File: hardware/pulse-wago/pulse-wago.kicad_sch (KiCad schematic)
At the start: 44 parts, among them J101 Cortex, SW101 SKSG, SW102 SKSG, U101 ATSAMD51J, U102 TPS78433QWDRBRQ1, Y101 32k768

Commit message: Refresh
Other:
- note added: "Solenoid Channels / Power +28V"
- note removed: "Solenoid Channels / Power +24V"
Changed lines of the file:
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@@
 		)
 	)
-	(text "Solenoid Channels / Power +24V"
+	(text "Solenoid Channels / Power +28V"
 		(exclude_from_sim no)
 		(at 153.035 16.51 0)

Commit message: Refresh
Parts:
- C107, C108: Manufacturer YAGEO -> TDK; Mouser 603-CC603JRNPO9BN180 -> 810-CGA3E2C0G1H180J; Product CC0603JRNPO9BN180 -> CGA3E2C0G1H180J080AA
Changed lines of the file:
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@@
 	(title_block
 		(title "V2 pulse WAGO")
-		(date "2026-02-10")
+		(date "2026-03-04")
 		(rev "2025-10-27")
 		(company "Versio Duo")
@@
 		(at 184.785 170.18 0)
 		(unit 1)
-		(exclude_from_sim yes)
+		(exclude_from_sim no)
 		(in_bom no)
 		(on_board yes)
@@
 			)
 		)
+		(property "Sim.Enable" "0"
+			(at 184.785 170.18 0)
+			(effects
+				(font
+					(size 1.27 1.27)
+				)
+				(hide yes)
+			)
+		)
 		(instances
 			(project "pulse"
@@
 		(at 218.44 151.13 0)
 		(unit 1)
-		(exclude_from_sim yes)
+		(exclude_from_sim no)
 		(in_bom no)
 		(on_board yes)
@@
 			)
 		)
+		(property "Sim.Enable" "0"
+			(at 218.44 151.13 0)
+			(effects
+				(font
+					(size 1.27 1.27)
+				)
+				(hide yes)
+			)
+		)
 		(instances
 			(project "pulse"
@@
 		(at 184.785 151.765 0)
 		(unit 1)
-		(exclude_from_sim yes)
+		(exclude_from_sim no)
 		(in_bom no)
 		(on_board yes)
@@
 			)
 		)
+		(property "Sim.Enable" "0"
+			(at 184.785 151.765 0)
+			(effects
+				(font
+					(size 1.27 1.27)
+				)
+				(hide yes)
+			)
+		)
 		(instances
 			(project "pulse"
@@
 		(at 218.44 157.48 0)
 		(unit 1)
-		(exclude_from_sim yes)
+		(exclude_from_sim no)
 		(in_bom no)
 		(on_board yes)
@@
 			)
 		)
+		(property "Sim.Enable" "0"
+			(at 218.44 157.48 0)
+			(effects
+				(font
+					(size 1.27 1.27)
+				)
+				(hide yes)
+			)
+		)
 		(instances
 			(project ""
@@
 			)
 		)
-		(property "Mouser" "603-CC603JRNPO9BN180"
+		(property "Mouser" "810-CGA3E2C0G1H180J"
 			(at 26.67 70.358 0)
 			(effects
@@
 			)
 		)
-		(property "Product" "CC0603JRNPO9BN180"
+		(property "Product" "CGA3E2C0G1H180J080AA"
 			(at 26.67 67.564 0)
 			(effects
@@
 			)
 		)
-		(property "Manufacturer" "YAGEO"
+		(property "Manufacturer" "TDK"
 			(at 26.67 64.77 0)
 			(effects
@@
 		(at 158.75 161.925 0)
 		(unit 1)
-		(exclude_from_sim yes)
+		(exclude_from_sim no)
 		(in_bom no)
 		(on_board yes)
@@
 			)
 		)
+		(property "Sim.Enable" "0"
+			(at 158.75 161.925 0)
+			(effects
+				(font
+					(size 1.27 1.27)
+				)
+				(hide yes)
+			)
+		)
 		(instances
 			(project "pulse"
@@
 			)
 		)
-		(property "Mouser" "603-CC603JRNPO9BN180"
+		(property "Mouser" "810-CGA3E2C0G1H180J"
 			(at 21.59 70.358 0)
 			(effects
@@
 			)
 		)
-		(property "Product" "CC0603JRNPO9BN180"
+		(property "Product" "CGA3E2C0G1H180J080AA"
 			(at 21.59 67.564 0)
 			(effects
@@
 			)
 		)
-		(property "Manufacturer" "YAGEO"
+		(property "Manufacturer" "TDK"
 			(at 21.59 64.77 0)
 			(effects
@@
 		(at 218.44 163.83 0)
 		(unit 1)
-		(exclude_from_sim yes)
+		(exclude_from_sim no)
 		(in_bom no)
 		(on_board yes)
@@
 			)
 		)
+		(property "Sim.Enable" "0"
+			(at 218.44 163.83 0)
+			(effects
+				(font
+					(size 1.27 1.27)
+				)
+				(hide yes)
+			)
+		)
 		(instances
 			(project ""
@@
 		(at 184.785 161.29 0)
 		(unit 1)
-		(exclude_from_sim yes)
+		(exclude_from_sim no)
 		(in_bom no)
 		(on_board yes)
@@
 			(at 184.785 161.29 0)
 			(effects
+				(font
+					(size 1.27 1.27)
+				)
+				(hide yes)
+			)
+		)
+		(property "Sim.Enable" "0"
+			(at 184.785 161.29 0)
+			(effects

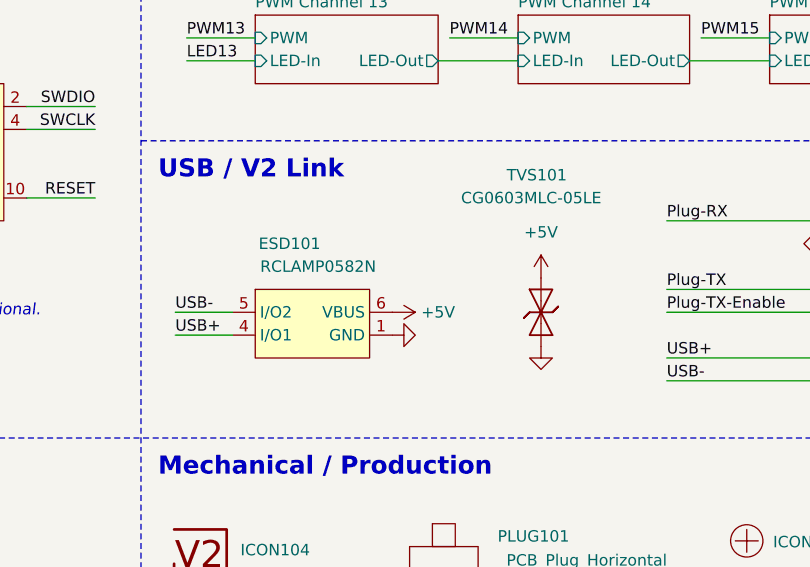
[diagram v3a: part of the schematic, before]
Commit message: Update ESD suppressor
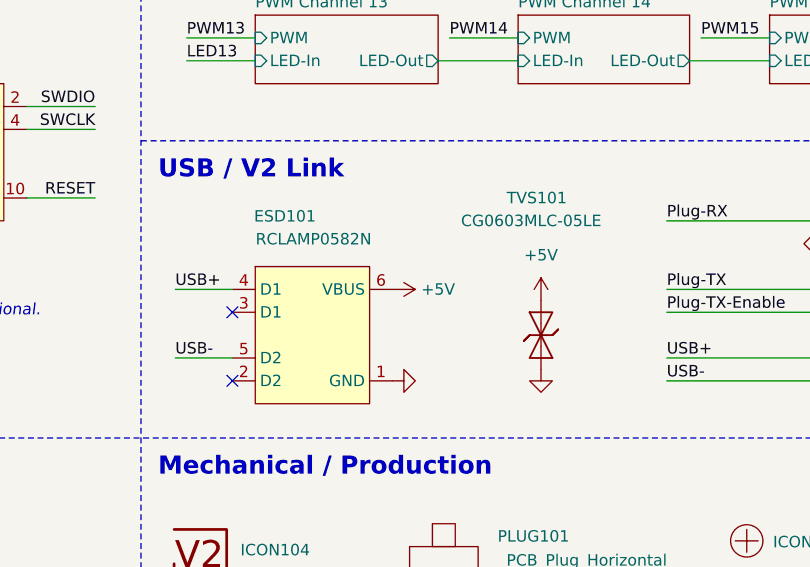
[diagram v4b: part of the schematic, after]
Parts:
- INFO102: value (none) -> ~
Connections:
- no-connect marks 16 -> 18
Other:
- moved on the sheet: TVS101

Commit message: Replace diode
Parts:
- INFO102: value ~ -> (none)

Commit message: Update
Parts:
- C101: renamed from C107; Id (none) -> Capacitor:${SYMBOL_NAME}; Rating (none) -> 50V
- C102: renamed from C108; Id (none) -> Capacitor:${SYMBOL_NAME}; Rating (none) -> 50V
- C103: renamed from C109; Id (none) -> Capacitor:${SYMBOL_NAME}
- C104: renamed from C101; Id (none) -> Capacitor:${SYMBOL_NAME}
- C105: renamed from C110; Id (none) -> Capacitor:${SYMBOL_NAME}
- C106: renamed from C102; Id (none) -> Capacitor:${SYMBOL_NAME}
- C107: renamed from C103; Id (none) -> Capacitor:${SYMBOL_NAME}
- C108: renamed from C104; Id (none) -> Capacitor:${SYMBOL_NAME}
- C109: renamed from C105; Id (none) -> Capacitor:${SYMBOL_NAME}
- C110: renamed from C106; Id (none) -> Capacitor:${SYMBOL_NAME}
- D101: renamed from D102; Id (none) -> LED:${SYMBOL_NAME}; Rating (none) -> 15mA
- D102: renamed from D101; Id (none) -> LED:${SYMBOL_NAME}; Rating (none) -> 605nm
- D103: Id (none) -> LED:${SYMBOL_NAME}; Rating (none) -> 15mA
- ESD101: Id (none) -> ESD:${SYMBOL_NAME}; Rating (none) -> 20kV
- R101: renamed from R102; Id (none) -> Resistor:${SYMBOL_NAME}
- R102: renamed from R101; Id (none) -> Resistor:${SYMBOL_NAME}
- SW101: renamed from SW102; Id (none) -> Button:${SYMBOL_NAME}; Rating (none) -> 1.6N
- SW102: renamed from SW101; Id (none) -> Button:${SYMBOL_NAME}; Rating (none) -> 1.6N
- TVS101: Id (none) -> Diode:${SYMBOL_NAME}
- U101: renamed from U102; Id (none) -> LDO:${SYMBOL_NAME}; Rating (none) -> 300mA
- U102: renamed from U101; Id (none) -> MCU:${SYMBOL_NAME}; Rating (none) -> Cortex-M4F
- Y101: Id (none) -> Crystal:${SYMBOL_NAME}; Rating (none) -> 10ppm
- renumbered H103 to H102, H105 to H103, H107 to H104, H108 to H105, H102 to H106, H104 to H107, H106 to H108, ICON104 to ICON101, ICON105 to ICON102, ICON101 to ICON103, ICON102 to ICON104, ICON103 to ICON105

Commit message: Good Bye Imperial
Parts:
- C101, C102: footprint V2_Capacitor_SMD:C_0603 -> V2_Capacitor_SMD:C_1608; symbol V2_Capacitor:0603_18p -> V2_Capacitor:1608_18p
- C103, C105: footprint V2_Capacitor_SMD:C_0805 -> V2_Capacitor_SMD:C_2012; symbol V2_Capacitor:0805_10u -> V2_Capacitor:2012_10u
- C104: footprint V2_Capacitor_SMD:C_0603 -> V2_Capacitor_SMD:C_1608; symbol V2_Capacitor:0603_10u -> V2_Capacitor:1608_10u
- C106, C107, C108, C109, C110: footprint V2_Capacitor_SMD:C_0603 -> V2_Capacitor_SMD:C_1608; symbol V2_Capacitor:0603_0u1 -> V2_Capacitor:1608_0u1
- D102: symbol V2_LED:0603_Orange -> V2_LED:1608_Orange
- R101: footprint V2_Resistor_SMD:R_0603 -> V2_Resistor_SMD:R_1608; symbol V2_Resistor:0603_100k -> V2_Resistor:1608_100k
- R102: footprint V2_Resistor_SMD:R_0603 -> V2_Resistor_SMD:R_1608; symbol V2_Resistor:0603_330R -> V2_Resistor:1608_330R
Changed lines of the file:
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@@
 	)
 	(symbol
-		(lib_id "V2_Capacitor:0603_0u1")
+		(lib_id "V2_Capacitor:1608_0u1")
 		(at 109.22 24.13 0)
 		(unit 1)
@@
 			)
 		)
-		(property "Footprint" "V2_Capacitor_SMD:C_0603"
+		(property "Footprint" "V2_Capacitor_SMD:C_1608"
 			(at 109.22 41.148 0)
 			(hide yes)
@@
 	)
 	(symbol
-		(lib_id "V2_LED:0603_Orange")
+		(lib_id "V2_LED:1608_Orange")
 		(at 125.73 86.36 0)
 		(mirror y)
@@
 	)
 	(symbol
-		(lib_id "V2_Capacitor:0805_10u")
+		(lib_id "V2_Capacitor:2012_10u")
 		(at 58.42 168.91 0)
 		(unit 1)
@@
 			)
 		)
-		(property "Footprint" "V2_Capacitor_SMD:C_0805"
+		(property "Footprint" "V2_Capacitor_SMD:C_2012"
 			(at 58.42 185.928 0)
 			(hide yes)
@@
 	)
 	(symbol
-		(lib_id "V2_Capacitor:0603_0u1")
+		(lib_id "V2_Capacitor:1608_0u1")
 		(at 119.38 24.13 0)
 		(unit 1)
@@
 			)
 		)
-		(property "Footprint" "V2_Capacitor_SMD:C_0603"
+		(property "Footprint" "V2_Capacitor_SMD:C_1608"
 			(at 119.38 41.148 0)
 			(hide yes)
@@
 	)
 	(symbol
-		(lib_id "V2_Capacitor:0805_10u")
+		(lib_id "V2_Capacitor:2012_10u")
 		(at 33.02 168.91 0)
 		(unit 1)
@@
 			)
 		)
-		(property "Footprint" "V2_Capacitor_SMD:C_0805"
+		(property "Footprint" "V2_Capacitor_SMD:C_2012"
 			(at 33.02 185.928 0)
 			(hide yes)
@@
 	)
 	(symbol
-		(lib_id "V2_Capacitor:0603_18p")
+		(lib_id "V2_Capacitor:1608_18p")
 		(at 26.67 46.99 0)
 		(unit 1)
@@
 			)
 		)
-		(property "Footprint" "V2_Capacitor_SMD:C_0603"
+		(property "Footprint" "V2_Capacitor_SMD:C_1608"
 			(at 26.67 64.008 0)
 			(hide yes)
@@
 	)
 	(symbol
-		(lib_id "V2_Capacitor:0603_10u")
+		(lib_id "V2_Capacitor:1608_10u")
 		(at 57.15 24.13 0)
 		(unit 1)
@@
 			)
 		)
-		(property "Footprint" "V2_Capacitor_SMD:C_0603"
+		(property "Footprint" "V2_Capacitor_SMD:C_1608"
 			(at 57.15 41.148 0)
 			(hide yes)
@@
 	)
 	(symbol
-		(lib_id "V2_Capacitor:0603_18p")
+		(lib_id "V2_Capacitor:1608_18p")
 		(at 21.59 46.99 0)
 		(unit 1)
@@
 			)
 		)
-		(property "Footprint" "V2_Capacitor_SMD:C_0603"
+		(property "Footprint" "V2_Capacitor_SMD:C_1608"
 			(at 21.59 64.008 0)
 			(hide yes)
@@
 	)
 	(symbol
-		(lib_id "V2_Resistor:0603_330R")
+		(lib_id "V2_Resistor:1608_330R")
 		(at 134.62 86.36 90)
 		(unit 1)
@@
 			)
 		)
-		(property "Footprint" "V2_Resistor_SMD:R_0603"
+		(property "Footprint" "V2_Resistor_SMD:R_1608"
 			(at 150.368 86.36 0)
 			(hide yes)
@@
 	)
 	(symbol
-		(lib_id "V2_Capacitor:0603_0u1")
+		(lib_id "V2_Capacitor:1608_0u1")
 		(at 99.06 24.13 0)
 		(unit 1)
@@
 			)
 		)
-		(property "Footprint" "V2_Capacitor_SMD:C_0603"
+		(property "Footprint" "V2_Capacitor_SMD:C_1608"
 			(at 99.06 41.148 0)
 			(hide yes)
@@
 	)
 	(symbol
-		(lib_id "V2_Capacitor:0603_0u1")
+		(lib_id "V2_Capacitor:1608_0u1")
 		(at 78.74 24.13 0)
 		(unit 1)
@@
 			)
 		)
-		(property "Footprint" "V2_Capacitor_SMD:C_0603"
+		(property "Footprint" "V2_Capacitor_SMD:C_1608"
 			(at 78.74 41.148 0)
 			(hide yes)
@@
 	)
 	(symbol
-		(lib_id "V2_Capacitor:0603_0u1")
+		(lib_id "V2_Capacitor:1608_0u1")
 		(at 88.9 24.13 0)
 		(unit 1)
@@
 			)
 		)
-		(property "Footprint" "V2_Capacitor_SMD:C_0603"
+		(property "Footprint" "V2_Capacitor_SMD:C_1608"
 			(at 88.9 41.148 0)
 			(hide yes)
@@
 	)
 	(symbol
-		(lib_id "V2_Resistor:0603_100k")
+		(lib_id "V2_Resistor:1608_100k")
 		(at 50.8 121.92 90)
 		(unit 1)
@@
 			)
 		)
-		(property "Footprint" "V2_Resistor_SMD:R_0603"
+		(property "Footprint" "V2_Resistor_SMD:R_1608"
 			(at 66.548 121.92 0)
 			(hide yes)

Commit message: Switch to 6 layer
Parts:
- D102: footprint V2_LED:LED_0603 -> V2_LED:LED_1608
- INFO101: value Layer_Numbers -> Layer_Numbers-6; footprint V2_Production:Layer_Numbers -> V2_Production:Layer_Numbers-6; symbol V2_Production:Layer_Numbers -> V2_Production:Layer_Numbers-6
- TVS101: footprint V2_Diode_SMD:D_0603 -> V2_Diode_SMD:D_1608
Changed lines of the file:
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@@
 	(title_block
 		(title "V2 pulse WAGO")
-		(date "2026-04-14")
-		(rev "2026-04-14")
+		(date "2026-06-08")
+		(rev "2026-06-08")
 		(company "Versio Duo")
 		(comment 1 "Solenoid Controller")
@@
 			)
 		)
-		(property "Footprint" "V2_LED:LED_0603"
+		(property "Footprint" "V2_LED:LED_1608"
 			(at 125.73 86.36 90)
 			(hide yes)
@@
 			)
 		)
-		(property "Footprint" "V2_Diode_SMD:D_0603"
+		(property "Footprint" "V2_Diode_SMD:D_1608"
 			(at 201.295 128.27 0)
 			(hide yes)
@@
 	)
 	(symbol
-		(lib_id "V2_Production:Layer_Numbers")
+		(lib_id "V2_Production:Layer_Numbers-6")
 		(at 159.385 171.45 0)
 		(unit 1)
@@
 			)
 		)
-		(property "Value" "Layer_Numbers"
+		(property "Value" "Layer_Numbers-6"
 			(at 158.7834 167.9785 0)
 			(hide yes)
@@
 			)
 		)
-		(property "Footprint" "V2_Production:Layer_Numbers"
+		(property "Footprint" "V2_Production:Layer_Numbers-6"
 			(at 159.385 177.8 0)
 			(hide yes)
@@
 			(name "V2_A4.kicad_wks")
 			(type worksheet)
-			(data |KLUv/WD5BbUPADbXSyEA1TbWikhSlOA2eC2ekVMEUCwq7NEwtcLUrO9RVbWigglBAD0ARQB3rDJr
-				Vfe8iEc347HKLOu3hM0n3acAgEAZ+mtWq1rqUSxebyypb/3fvvl2Ks1ai1318qyxua+IAgRM0MgT
-				vxCDqNazy01dUkv9SffBzyqWXV6zk7TDjC//75ZXzHffvHX4Y/Xf35uU+iW//OHdpP7XYKnf08G7
-				Ws+4sz/Se05W5tbSsFNFN3RTUXTjhdPWNR7ehuG4iIngvhBQHGxi+IlSiXCRzHYxEfbe576fb+gn
-				B78Z+mSX28Z5ZV5BEKwWAwQ+a06BCmH90rZJg9JtG4SrtqNsE+pn/kpSOzSUhmVScSgcO1gJcdSg
-				J6zLuq1W1TZJF+moiP3v9XDUP1+S1KFCs7SB4TTQalSg4UCjGDM0M3GaNAZgZObmWAewpQGB0gB3
-				GYWe0WuYLYxil2+HCVPCLoewmMo8a9CJow+hHPOLKHdUb0wU8lRpRE+qFdAXJgbU7nMwecZYivJQ
-				iTgLkNig5tH7xtAJA8QyZ+ZP4GUJKSTwm+RM51H7yWknvCe7YZZxrISdEQ48yLJBiQaevBZD1kY4
-				h0V7Dqlt/1rBcP0NQy83g9hYapcpANydipsbWw09qO7ggsG8qpSEBRoltBf/e9cTMh29AaQeYKo=|
+			(data |KLUv/WABBs0PAPaWSyEA1TbWikhSlOA2eC2ekVMEUCwq7NEwtcLUrO9RVbWigglBAD0ARABjlVmr
+				uudFPLoZj1VmWb8lbD7pPgUABMrQX7Na1VKPYvF6Y0l96//2zbdTadZa7KqXZ43NfUUUIGCCRp74
+				hRhEBdnlpi6ppf6k++BnFcsur9lJ2mHGl/93yyvmu2/eOvyx+u/vTUr9kl/+8G5S/2uw1O/p4F2t
+				Z9zZH+k95wbVytxaGnaq6KaiClvXeHgbhuMi7guB082G4mATw0+USoSLZLaLibD3Pvf9fEM/OfjN
+				0Ce73DbOK/MKgmC1GCDwWXOsB4EKYf3StkmD0m0bhKu2o2wT6mf+SlI7NJSGZVJxKBw7WAlx1KAn
+				rMu6rVbVNkkX6aiI/e/1cNQ/X5LUoUKztIHhNNACV6ABRYOUmppZnDRrYGTm5lgHuKUBCqUheRmB
+				mtErmC2cYpdvw4QpAS+HW0x9ni3oxOjDIsfMJMoe1TEVRT9Vsuj5tcL6QokDa/DzUfliHjoPDuAp
+				yB0UltwFSGjQ8qh9YsiEAU6ZM/MH8LbEFFL4TXKm8ij9cNrJ7wlu2DKOnbAzzIEHWY4okcCT1GJg
+				bYhzrGivkMr2LxUEt7459HIzhg2rdlkB6u5W3N7YeuhB6m4vyMxrpWQtkChBv9Dfi56Y6YgbQOoB
+				pgo=|
 			)
-			(checksum "080A27BD1FADC1F81518BF82EA92C143")
+			(checksum "6080E9E16B39514519B8031C50AB7B2F")
 		)
 	)
